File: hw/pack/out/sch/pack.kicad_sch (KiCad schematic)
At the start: 0 parts

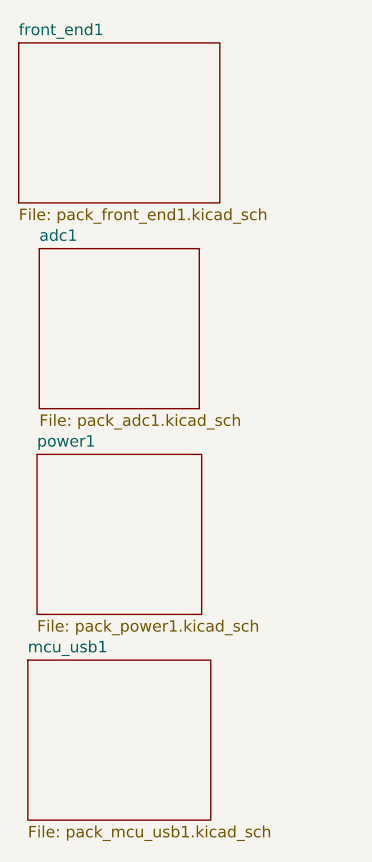
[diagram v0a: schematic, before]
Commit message: pack: cost-down to PK-12 $33.34: printed cell cradle + MYOUNG contacts, LCSC IPEX pigtail, priced M2 screws (#34)
- BT1: MYOUNG MY-18650-04-J/-05-J (LCSC C19184125/C19184124) in a printed
  cradle in the base (76 mm plate faces: spring 4.2-9.2 mm for 70-65 mm cells);
  the SMT BH-18650-B1BA002 holder is gone; footprint Cell_Wire_Pads
- pigtail: BAT Wireless BWIPX1-SMA-1.13L150 (LCSC C784404, $0.6015 @100), SMA
  cut off, ~100 mm + 31 mm wire whip; audit.py PIGTAIL_IL 0.46 <= 0.6 dB
- audit.py cutoff path includes the spring (0.10 ohm), cutoff stays 3.2 V
- 2 x M2x6 PT screws $0.112 (Fastener Superstore 585907)
- prices.py, bom.csv, pack_uk.csv (UK $34.81) updated

Co-Authored-By: Claude Opus 5.5 <noreply@anthropic.com>
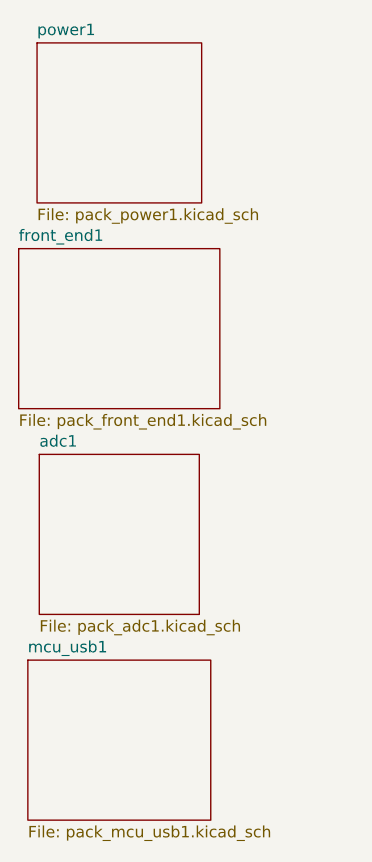
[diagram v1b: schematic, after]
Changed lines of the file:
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@@
   (title_block
     (title "OpenPack body-pack")
-    (date "2026-10-31")
+    (date "2026-11-01")
     (company "")
     (comment 1 "Generated with SKiDL")
@@
     (comment 4 ""))
   (sheet
-    (at 139.45 107.95)
+    (at 139.45 62.23)
     (size 18.29 17.78)
     (exclude_from_sim no)
@@
       (color 0 0 0 0.0))
     (property "Sheetname" "power1"
-      (at 139.45 107.24 0)
+      (at 139.45 61.52 0)
       (effects
         (font
@@
         (justify left bottom)))
     (property "Sheetfile" "pack_power1.kicad_sch"
-      (at 139.45 126.31 0)
+      (at 139.45 80.59 0)
       (effects
         (font
@@
         (justify left top))))
   (sheet
-    (at 137.41 62.23)
+    (at 137.41 85.09)
     (size 22.35 17.78)
     (exclude_from_sim no)
@@
       (color 0 0 0 0.0))
     (property "Sheetname" "front_end1"
-      (at 137.41 61.52 0)
+      (at 137.41 84.38 0)
       (effects
         (font
@@
         (justify left bottom)))
     (property "Sheetfile" "pack_front_end1.kicad_sch"
-      (at 137.41 80.59 0)
+      (at 137.41 103.45 0)
       (effects
         (font
@@
         (justify left top))))
   (sheet
-    (at 139.7 85.09)
+    (at 139.7 107.95)
     (size 17.78 17.78)
     (exclude_from_sim no)
@@
       (color 0 0 0 0.0))
     (property "Sheetname" "adc1"
-      (at 139.7 84.38 0)
+      (at 139.7 107.24 0)
       (effects
         (font
@@
         (justify left bottom)))
     (property "Sheetfile" "pack_adc1.kicad_sch"
-      (at 139.7 103.45 0)
+      (at 139.7 126.31 0)
       (effects
         (font
